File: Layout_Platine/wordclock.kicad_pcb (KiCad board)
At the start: 2 copper layers, 80 x 50.8 mm, 68 parts, among them IC1 ATmega8, P1 DCF_CONN_4, P10 CONN_1, P13 P_led, P14 CONN_2, P2 5V_CONN_2, P3 ISP, P4 UART_CONN_6, P5 Led_Zeilen_CONN_11, P6 Led_Spalten_CONN_11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

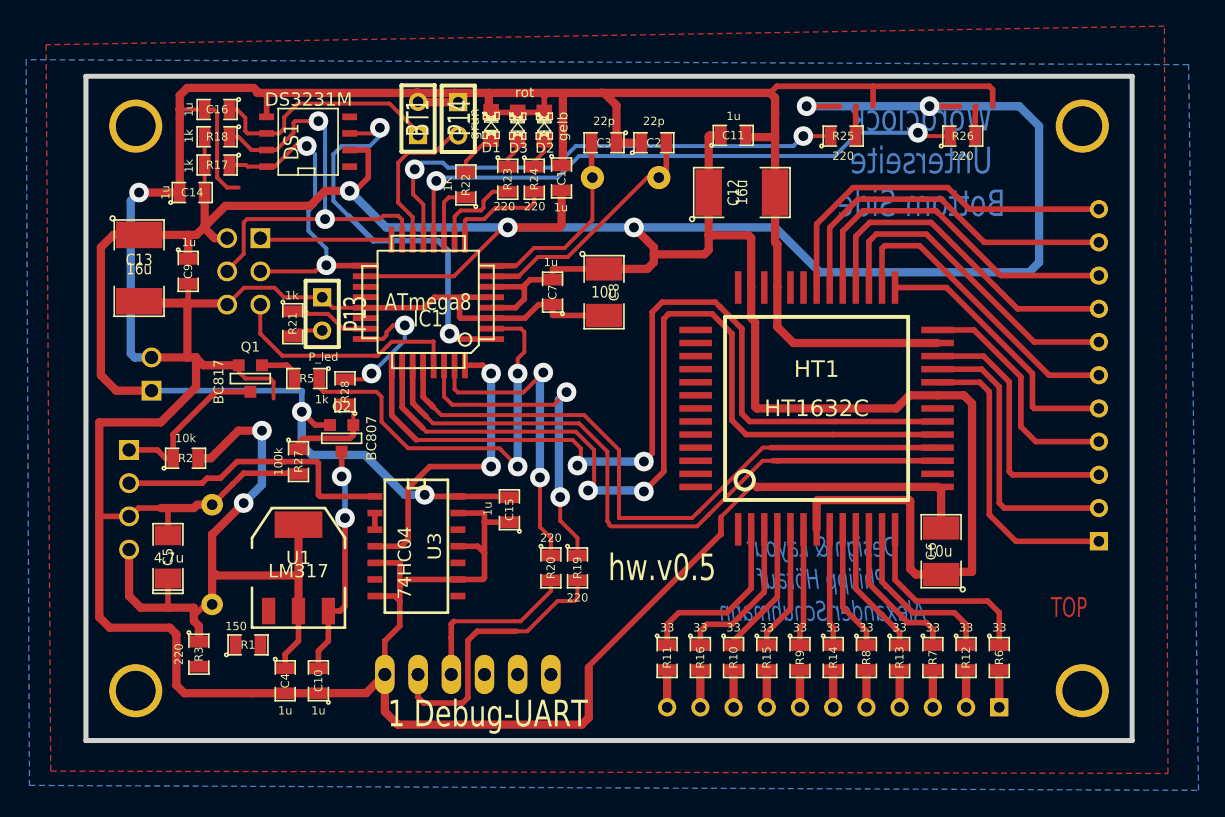
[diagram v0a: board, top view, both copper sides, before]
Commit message: HardwareVersion 5 an sich fertig zur Herstellung. nur noch kleinere Änderungen, keine weiteren Features mehr.
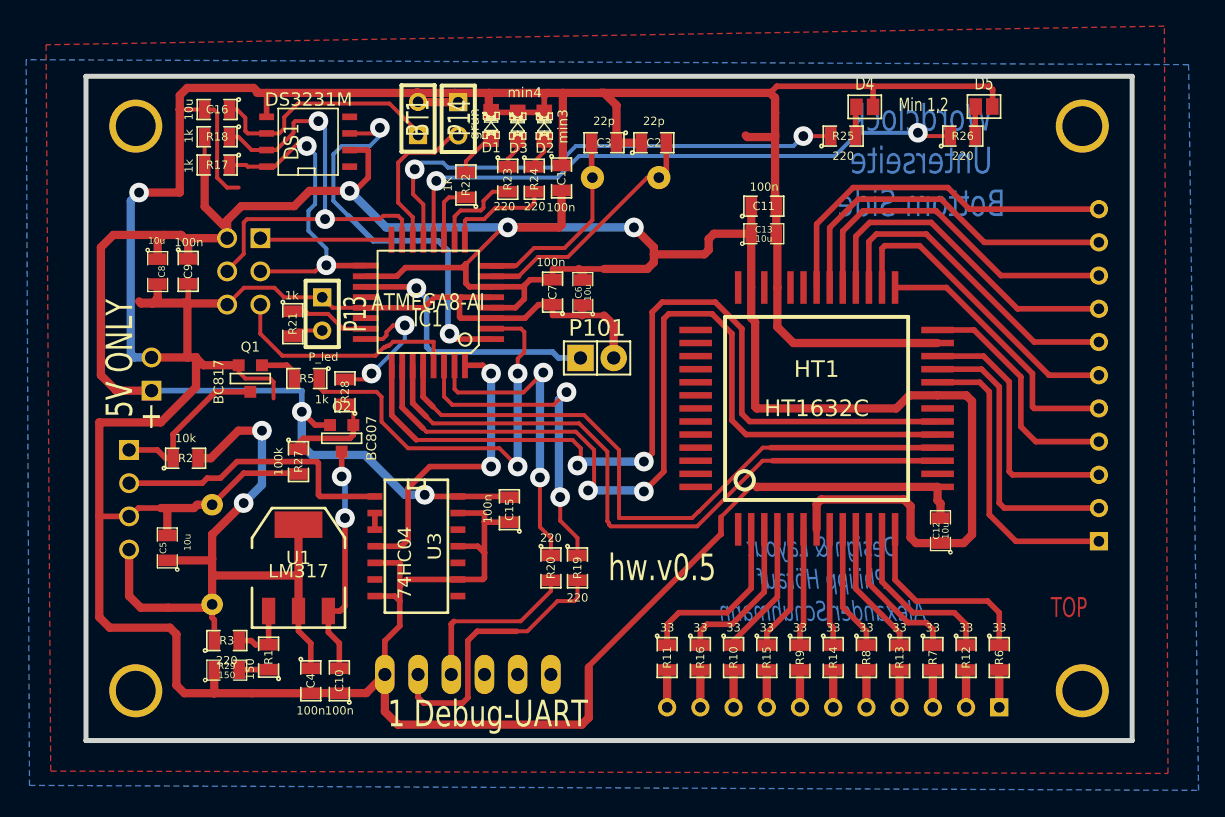
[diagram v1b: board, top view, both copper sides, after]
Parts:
- removed C14: 1u, SM0805
- added D4: min1, Connect:GS2, F.Cu at (229.7, 39.2)
- added D5: min2, Connect:GS2, F.Cu at (238.9, 39.1)
- added P101: CONN_01X02, Pin_Headers:Pin_Header_Straight_1x02, F.Cu at (209.3, 58.4)
- added R29: 150, SMD_Packages:SMD-0805, F.Cu at (180.9, 82.2)
- C1, C10, C11, C15, C4, C7, C9: value 1u -> 100n
- C12, C13: value 16u -> 10u; footprint SM1812L -> SMD_Packages:SMD-0805
- C16: value 1u -> 10u
- C5: value 4,7u -> 10u; footprint SM1206POL -> SMD_Packages:SMD-0805
- C6, C8: footprint SM1210L -> SMD_Packages:SMD-0805
- D2: value gelb -> min3
- D3: value rot -> min4
- IC1: value ATmega8 -> ATMEGA8-AI
- R4: value 100 -> 150
- moved C13 47.8 mm to (222.0, 48.9), turned to 0 degrees
- moved C8 34.2 mm to (175.7, 51.8)
- moved C6 33.8 mm to (208.2, 53.4)
- moved C12 30.0 mm to (235.5, 71.6), turned to 90 degrees
- moved C11 5.89 mm to (222.0, 46.8)
- moved R3 2.37 mm to (180.9, 80.0), turned to 0 degrees
- moved C4 1.96 mm to (187.4, 83.1)
- moved R1 1.83 mm to (184.2, 81.3), turned to 90 degrees
- moved C10 1.60 mm to (189.6, 83.1)
- moved C5 0.69 mm to (176.4, 72.9)
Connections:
- C1 pad 2: +5V -> VCC
- C11 pad 1: +5V -> VCC
- C12 pad 1: +5V -> VCC
- C13 pad 1: +5V -> VCC
- C15 pad 2: +5V -> VCC
- C6 pad 1: +5V -> GND
- C6 pad 2: GND -> VCC
- C7 pad 2: +5V -> VCC
- C8 pad 1: +5V -> VCC
- C9 pad 1: +5V -> VCC
- DS1 pad 1: (no net) -> Net-(DS1-Pad1)
- DS1 pad 2: +5V -> VCC
- DS1 pad 4: (no net) -> Net-(DS1-Pad4)
- HT1 pad 1: (no net) -> Net-(HT1-Pad1)
- HT1 pad 15: (no net) -> Net-(HT1-Pad15)
- HT1 pad 20: (no net) -> Net-(HT1-Pad20)
- HT1 pad 21: +5V -> VCC
- HT1 pad 34: (no net) -> Net-(HT1-Pad34)
- HT1 pad 35: (no net) -> Net-(HT1-Pad35)
- HT1 pad 37: (no net) -> Net-(HT1-Pad37)
- HT1 pad 38: +5V -> VCC
- HT1 pad 39: (no net) -> Net-(HT1-Pad39)
- HT1 pad 40: (no net) -> Net-(HT1-Pad40)
- HT1 pad 41: (no net) -> Net-(HT1-Pad41)
- HT1 pad 42: (no net) -> Net-(HT1-Pad42)
- HT1 pad 43: (no net) -> Net-(HT1-Pad43)
- HT1 pad 44: (no net) -> Net-(HT1-Pad44)
- HT1 pad 45: (no net) -> Net-(HT1-Pad45)
- HT1 pad 46: (no net) -> Net-(HT1-Pad46)
- HT1 pad 47: (no net) -> Net-(HT1-Pad47)
- HT1 pad 48: (no net) -> Net-(HT1-Pad48)
- HT1 pad 49: (no net) -> Net-(HT1-Pad49)
- HT1 pad 50: (no net) -> Net-(HT1-Pad50)
- HT1 pad 51: (no net) -> Net-(HT1-Pad51)
- HT1 pad 52: (no net) -> Net-(HT1-Pad52)
- HT1 pad 7: +5V -> VCC
- IC1 pad 18: +5V -> VCC
- IC1 pad 19: (no net) -> /lichtsensor
- IC1 pad 20: (no net) -> Net-(C17-Pad1)
- IC1 pad 22: (no net) -> Net-(IC1-Pad22)
- IC1 pad 4: +5V -> VCC
- IC1 pad 6: +5V -> VCC
- P10 pad 1: (no net) -> Net-(P10-Pad1)
- P2 pad 1: +5V -> VCC
- P3 pad 2: +5V -> VCC
- P4 pad 4: (no net) -> Net-(P4-Pad4)
- P4 pad 5: (no net) -> Net-(P4-Pad5)
- P4 pad 6: (no net) -> Net-(P4-Pad6)
- P7 pad 1: (no net) -> Net-(P7-Pad1)
- P8 pad 1: (no net) -> Net-(P8-Pad1)
- P9 pad 1: (no net) -> Net-(P9-Pad1)
- Q2 pad 1: +5V -> VCC
- R1 pad 1: (no net) -> Net-(R1-Pad1)
- R17 pad 2: +5V -> VCC
- R18 pad 2: +5V -> VCC
- R25 pad 2: (no net) -> Net-(D4-Pad1)
- R26 pad 2: (no net) -> Net-(D5-Pad1)
- U3 pad 10: (no net) -> Net-(U3-Pad10)
- U3 pad 12: (no net) -> Net-(U3-Pad12)
- U3 pad 14: +5V -> VCC
- U3 pad 6: (no net) -> Net-(U3-Pad6)
- U3 pad 8: (no net) -> Net-(U3-Pad8)
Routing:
- net +5V: track 297.5 -> 0.00 mm, vias 7 -> 0
- net VCC: track 0.00 -> 226.2 mm, vias 0 -> 5
- net /lichtsensor: track 0.00 -> 20.8 mm, vias 0 -> 1
- net GND: track 394.4 -> 402.0 mm
- net Net-(R1-Pad2): track 0.00 -> 4.96 mm
- net (no net): track 4.62 -> 0.00 mm
- net Net-(D5-Pad1): track 0.00 -> 2.31 mm
- net Net-(D4-Pad1): track 0.00 -> 2.31 mm
- net Net-(R1-Pad1): track 0.00 -> 2.26 mm
- net Net-(IC1-Pad30): track 26.6 -> 25.7 mm
- net /3V: track 55.2 -> 56.0 mm
- net /mosi: track 35.0 -> 34.5 mm
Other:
- board text added: "+"
- board text added: "10 MHz"
- board text added: "5V ONLY"
- board text added: "Atmel ISP"
- board text added: "DCF"
- board text added: "Min 1,2"
- board text added: "STROM"

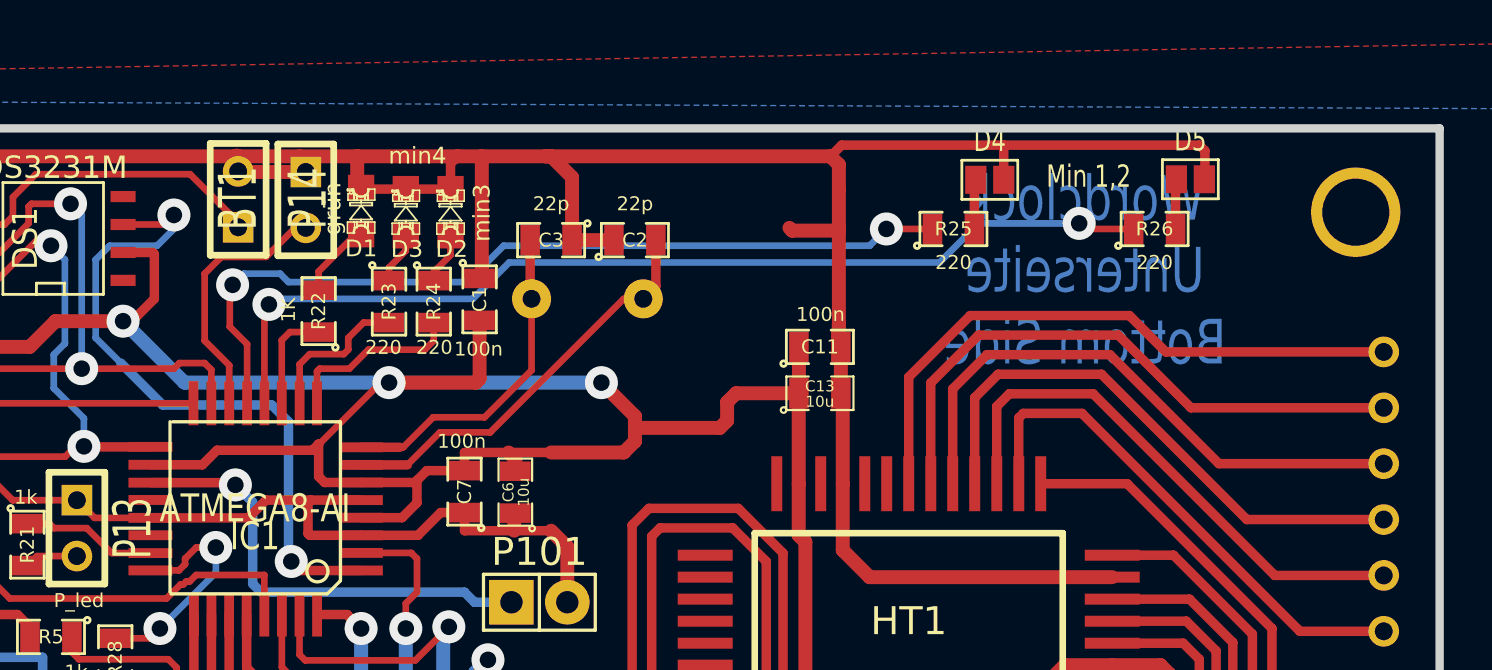
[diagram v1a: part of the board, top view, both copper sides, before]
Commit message: Minuten-LEDs jetzt mit Durchkontaktierung für bessere mechanische Stabilität.
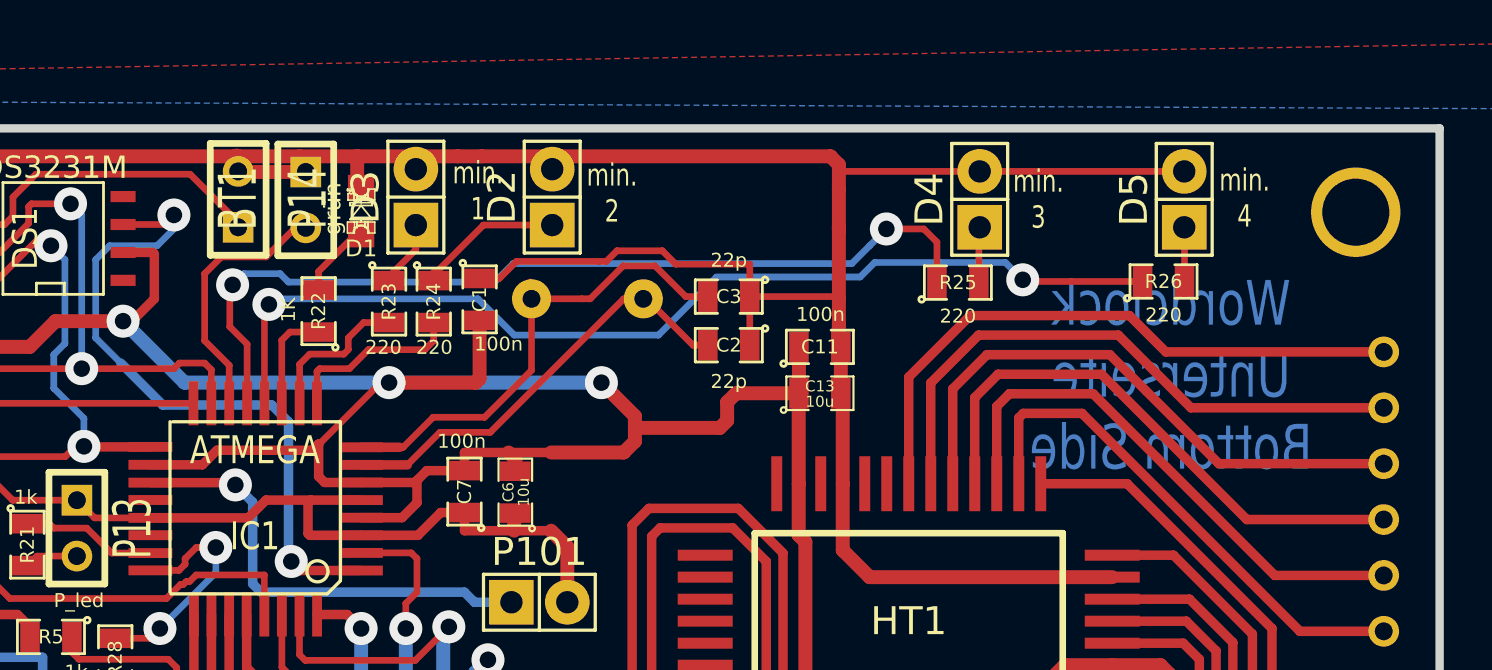
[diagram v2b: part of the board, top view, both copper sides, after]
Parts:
- D2, D3: footprint LED-0805-newMask -> Pin_Headers:Pin_Header_Straight_1x02
- D4, D5: footprint Connect:GS2 -> Pin_Headers:Pin_Header_Straight_1x02
- IC1: value ATMEGA8-AI -> ATMEGA
- moved C3 8.47 mm to (217.9, 44.5)
- moved C2 6.40 mm to (217.9, 46.7), turned to 180 degrees
- moved D2 4.67 mm to (209.9, 40.0)
- moved R25 2.45 mm to (228.3, 43.8)
- moved R26 2.42 mm to (237.6, 43.8)
- moved D4 1.00 mm to (229.3, 40.1)
- moved D5 0.96 mm to (238.6, 40.1)
- moved D3 0.82 mm to (203.7, 40.0)
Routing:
- net Net-(C3-Pad2): track 15.2 -> 22.4 mm
- net Net-(D2-Pad1): track 2.38 -> 6.98 mm
- net GND: track 402.0 -> 398.9 mm
- net /minuten_1: track 38.9 -> 41.2 mm
- net /minuten_2: track 45.5 -> 46.8 mm
- net Net-(C2-Pad2): track 18.9 -> 19.8 mm
- net Net-(D3-Pad1): track 2.38 -> 3.03 mm
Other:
- board text added: "min. 1"
- board text added: "min. 2"
- board text added: "min. 3"
- board text added: "min. 4"
- board text removed: "Min 1,2"

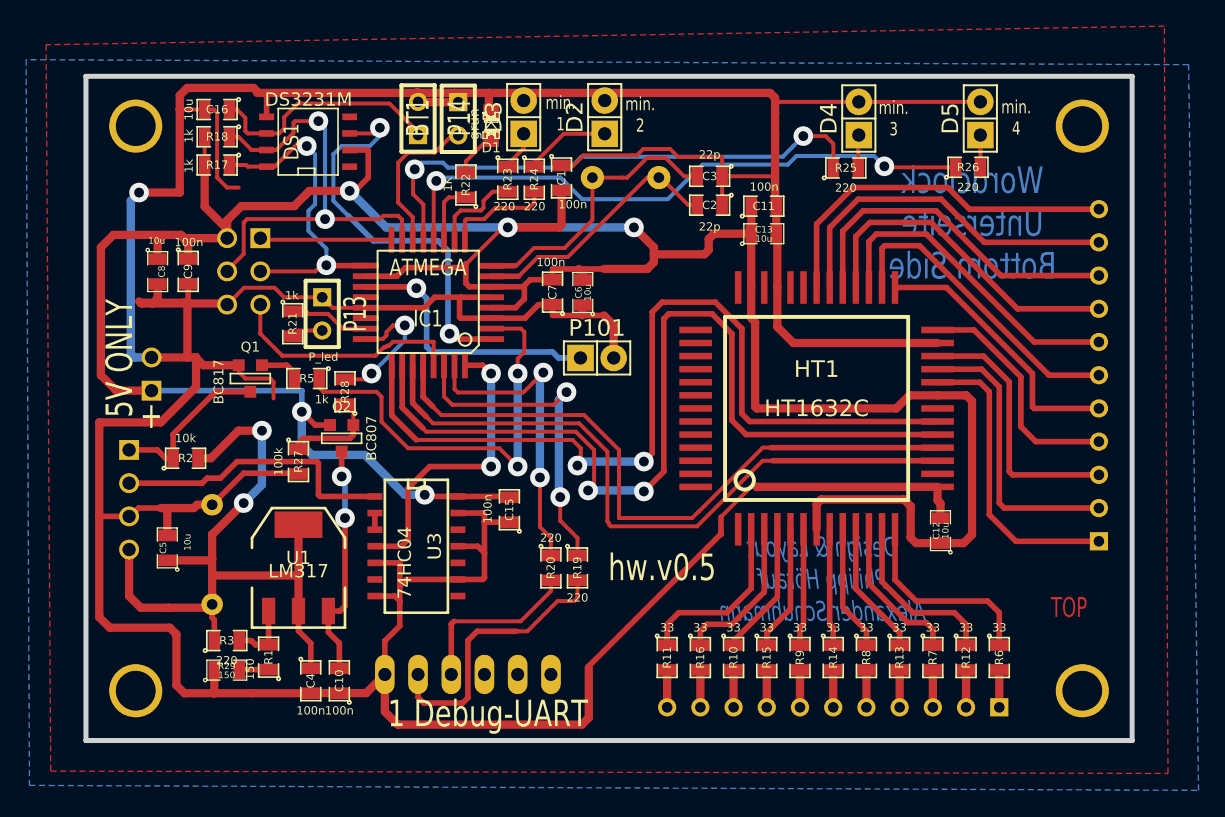
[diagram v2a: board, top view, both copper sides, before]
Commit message: max Änderungsvorschläge wurden fast komplett umgesetzt. nur das DCF-modul ist noch nicht im Bestückungsdruck vertreten. TODO.
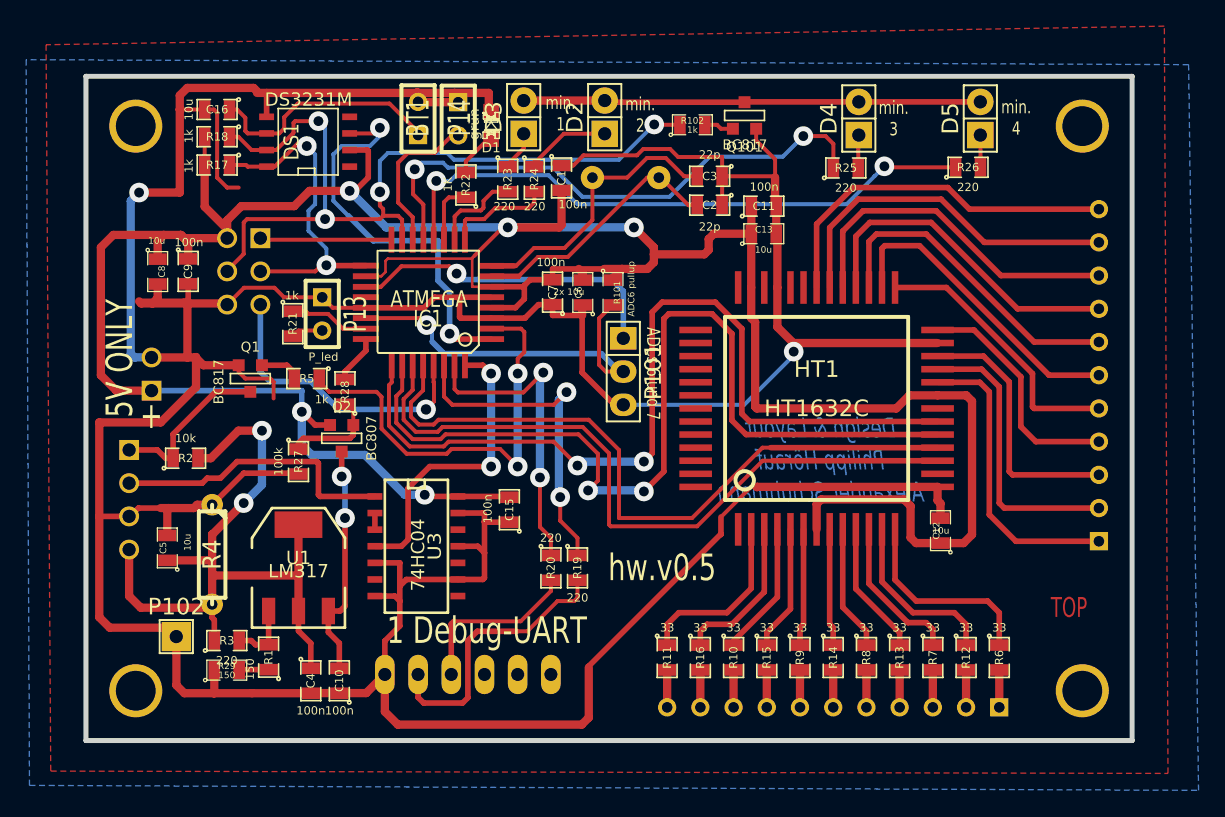
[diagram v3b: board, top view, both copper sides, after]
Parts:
- added P102: CONN_01X01, Pin_Headers:Pin_Header_Straight_1x01, F.Cu at (177.1, 79.7)
- added Q101: BC817, SMD_Packages:SOT-23-EBC, F.Cu at (220.5, 39.8)
- added R101: ADC6 pullup, SMD_Packages:SMD-0805, F.Cu at (210.5, 53.4)
- added R102: 1k, SMD_Packages:SMD-0805, F.Cu at (216.6, 40.5)
- C6: value 10u -> 2x 10u
- P101: value CONN_01X02 -> CONN_01X03; footprint Pin_Headers:Pin_Header_Straight_1x02 -> Pin_Headers:Pin_Header_Straight_1x03
- R4: moved to F.Cu
- moved P101 2.26 mm to (211.3, 59.4), turned to 270 degrees
- turned R4 to 270 degrees
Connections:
- net VCC renamed +5V
- D2 pad 2: GND -> Net-(D2-Pad2)
- D3 pad 2: GND -> Net-(D2-Pad2)
- D4 pad 2: GND -> Net-(D2-Pad2)
- D5 pad 2: GND -> Net-(D2-Pad2)
- IC1 pad 22: Net-(IC1-Pad22) -> /debug
- P101 pad 2: GND -> /debug
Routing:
- net Net-(D2-Pad2): track 0.00 -> 35.1 mm
- net /debug: track 0.00 -> 29.0 mm, vias 0 -> 1
- net /mosi: track 34.5 -> 63.4 mm, vias 2 -> 4
- net GND: track 398.9 -> 377.3 mm, vias 1 -> 2
- net /dcf_on: track 10.5 -> 3.75 mm, vias 2 -> 0
- net /reset: track 18.4 -> 22.7 mm, vias 0 -> 1
- net /lichtsensor: track 20.8 -> 24.7 mm
- net /WriteClock: track 50.9 -> 53.4 mm
- net Net-(Q101-Pad2): track 0.00 -> 2.27 mm
- net /SerialData: track 52.2 -> 54.3 mm
- net /ReadClock: track 69.5 -> 71.3 mm
- net /minuten_1: track 41.2 -> 43.1 mm
- net +5V: track 226.2 -> 228.0 mm
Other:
- board text added: "5V DC"
- board text added: "ADCs 6 und 7"
- board text added: "LED-Matrix Anoden (+)"
- board text added: "LED-Matrix Kathoden (-)"
- board text added: "Web: https://github.com/Virtex7/led-wordclock"
- board text removed: "STROM"
- board text removed: "Wordclock Unterseite Bottom Side"
